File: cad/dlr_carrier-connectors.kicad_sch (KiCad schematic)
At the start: 5 parts, among them J11 DEBUG_UART, J12 USBC_COMMISSIONING, J3 BAT

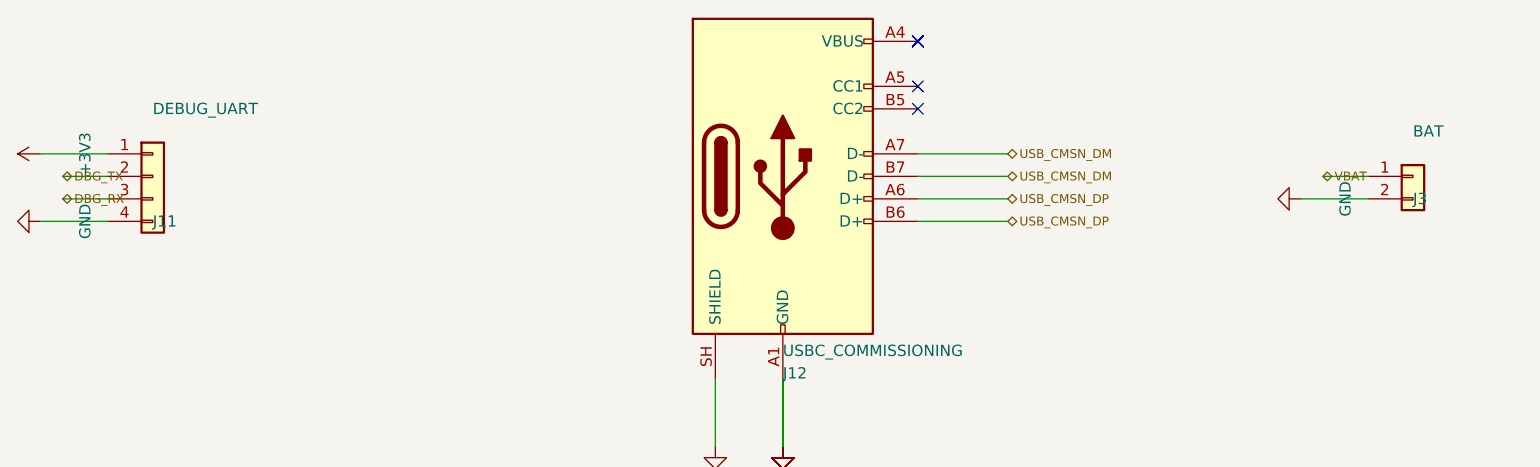
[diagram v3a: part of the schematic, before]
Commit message: 🩺 refactor(schematic): cross-sheet nets via global labels, no sheet pins
Three attempts at making the hierarchical sheet-pin mechanism pass KiCad 9 failed
(project name, instance paths, label type), so the mechanism goes. Cross-sheet nets
now connect by name through global labels on the child sheets; the root carries
sheet symbols only — no pins, no stub wires, no labels.

That removes the whole hier_label_mismatch / label_dangling class rather than
chasing it, and it matches the connectivity style the generate-schematic skill
already prescribes for this project ("all inter-block connections use net labels").

kicad-sch-api's add_global_label still does not serialize, so the labels are emitted
as hierarchical and rewritten in the saved sheet.

Co-Authored-By: Claude Opus 5 <noreply@anthropic.com>
Claude-Session: https://claude.ai/code/session_011xr7VCL7rkJj2WE2uQF7sF
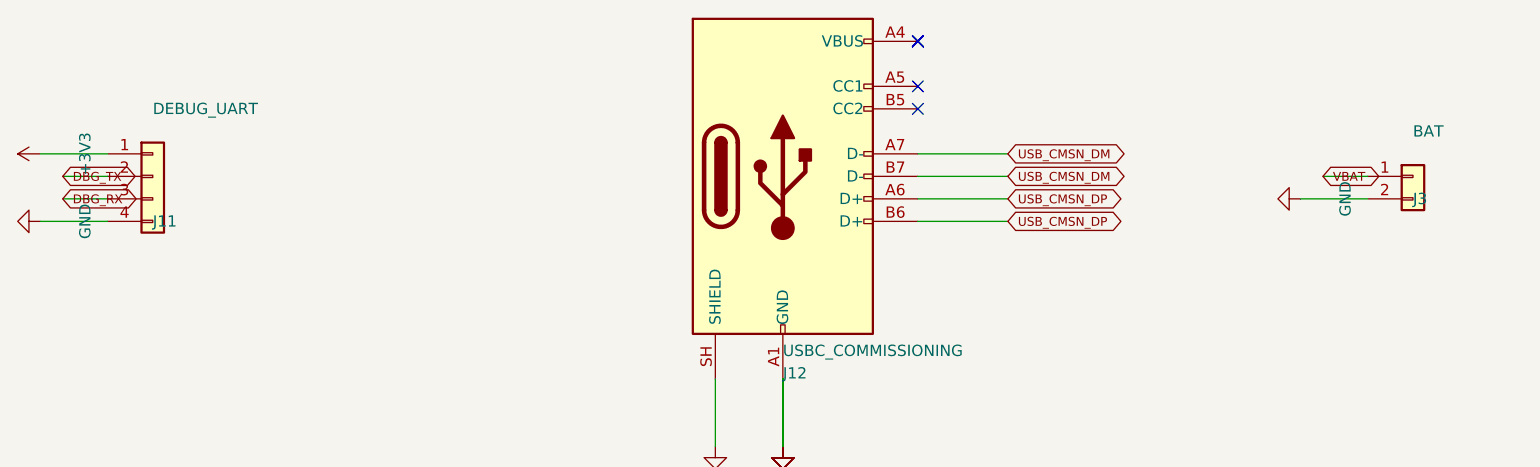
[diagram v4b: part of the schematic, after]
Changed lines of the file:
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@@
 		(instances
 			(project "CONNECTORS"
-				(path "/8192665d-bcfc-4432-b821-887d2ec6e9bf"
+				(path "/7d9d3fdc-ee14-434c-a81c-56c5137a4703"
 					(reference "J11")
 					(unit 1)
@@
 		(instances
 			(project "CONNECTORS"
-				(path "/8192665d-bcfc-4432-b821-887d2ec6e9bf"
+				(path "/7d9d3fdc-ee14-434c-a81c-56c5137a4703"
 					(reference "J12")
 					(unit 1)
@@
 		(instances
 			(project "CONNECTORS"
-				(path "/8192665d-bcfc-4432-b821-887d2ec6e9bf"
+				(path "/7d9d3fdc-ee14-434c-a81c-56c5137a4703"
 					(reference "J3")
 					(unit 1)
@@
 		(instances
 			(project "CONNECTORS"
-				(path "/8192665d-bcfc-4432-b821-887d2ec6e9bf"
+				(path "/7d9d3fdc-ee14-434c-a81c-56c5137a4703"
 					(reference "R12")
 					(unit 1)
@@
 		(instances
 			(project "CONNECTORS"
-				(path "/8192665d-bcfc-4432-b821-887d2ec6e9bf"
+				(path "/7d9d3fdc-ee14-434c-a81c-56c5137a4703"
 					(reference "R13")
 					(unit 1)
@@
 		(instances
 			(project "CONNECTORS"
-				(path "/8192665d-bcfc-4432-b821-887d2ec6e9bf"
+				(path "/7d9d3fdc-ee14-434c-a81c-56c5137a4703"
 					(reference "#PWR001")
 					(unit 1)
@@
 		(instances
 			(project "CONNECTORS"
-				(path "/8192665d-bcfc-4432-b821-887d2ec6e9bf"
+				(path "/7d9d3fdc-ee14-434c-a81c-56c5137a4703"
 					(reference "#PWR002")
 					(unit 1)
@@
 		(instances
 			(project "CONNECTORS"
-				(path "/8192665d-bcfc-4432-b821-887d2ec6e9bf"
+				(path "/7d9d3fdc-ee14-434c-a81c-56c5137a4703"
 					(reference "#PWR003")
 					(unit 1)
@@
 		(instances
 			(project "CONNECTORS"
-				(path "/8192665d-bcfc-4432-b821-887d2ec6e9bf"
+				(path "/7d9d3fdc-ee14-434c-a81c-56c5137a4703"
 					(reference "#PWR004")
 					(unit 1)
@@
 		(instances
 			(project "CONNECTORS"
-				(path "/8192665d-bcfc-4432-b821-887d2ec6e9bf"
+				(path "/7d9d3fdc-ee14-434c-a81c-56c5137a4703"
 					(reference "#PWR005")
 					(unit 1)
@@
 		(instances
 			(project "CONNECTORS"
-				(path "/8192665d-bcfc-4432-b821-887d2ec6e9bf"
+				(path "/7d9d3fdc-ee14-434c-a81c-56c5137a4703"
 					(reference "#PWR006")
 					(unit 1)
@@
 		(instances
 			(project "CONNECTORS"
-				(path "/8192665d-bcfc-4432-b821-887d2ec6e9bf"
+				(path "/7d9d3fdc-ee14-434c-a81c-56c5137a4703"
 					(reference "#PWR007")
 					(unit 1)
@@
 		(instances
 			(project "CONNECTORS"
-				(path "/8192665d-bcfc-4432-b821-887d2ec6e9bf"
+				(path "/7d9d3fdc-ee14-434c-a81c-56c5137a4703"
 					(reference "#PWR008")
 					(unit 1)
@@
 		(instances
 			(project "CONNECTORS"
-				(path "/8192665d-bcfc-4432-b821-887d2ec6e9bf"
+				(path "/7d9d3fdc-ee14-434c-a81c-56c5137a4703"
 					(reference "#PWR009")
 					(unit 1)
@@
 		(instances
 			(project "CONNECTORS"
-				(path "/8192665d-bcfc-4432-b821-887d2ec6e9bf"
+				(path "/7d9d3fdc-ee14-434c-a81c-56c5137a4703"
 					(reference "#PWR010")
 					(unit 1)
@@
 		)
 	)
-	(hierarchical_label "DBG_RX"
+	(global_label "DBG_RX"
 		(shape bidirectional)
 		(at 63.5 167.64 180)
@@
 		)
 	)
-	(hierarchical_label "DBG_TX"
+	(global_label "DBG_TX"
 		(shape bidirectional)
 		(at 63.5 165.1 180)
@@
 		)
 	)
-	(hierarchical_label "USB_CMSN_DM"
+	(global_label "USB_CMSN_DM"
 		(shape bidirectional)
 		(at 170.18 162.56 0)
@@
 		)
 	)
-	(hierarchical_label "USB_CMSN_DM"
+	(global_label "USB_CMSN_DM"
 		(shape bidirectional)
 		(at 170.18 165.1 0)
@@
 		)
 	)
-	(hierarchical_label "USB_CMSN_DP"
+	(global_label "USB_CMSN_DP"
 		(shape bidirectional)
 		(at 170.18 167.64 0)
@@
 		)
 	)
-	(hierarchical_label "USB_CMSN_DP"
+	(global_label "USB_CMSN_DP"
 		(shape bidirectional)
 		(at 170.18 170.18 0)
@@
 		)
 	)
-	(hierarchical_label "VBAT"
+	(global_label "VBAT"
 		(shape bidirectional)
 		(at 205.74 165.1 180)
@@
 	)
 	(sheet_instances
-		(path "/8c69d83a-4880-48ed-90c2-e87a41cb06f9"
+		(path "/4f3d8455-0574-4c61-9182-7c1ed837becf"
 			(page "7")
 		)
